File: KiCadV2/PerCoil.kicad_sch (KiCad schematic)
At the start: 22 parts, among them U14 74LV08AT14-13, U18 MX3502S, U22 DMHT10H032LFJ, U23 INA240A1D

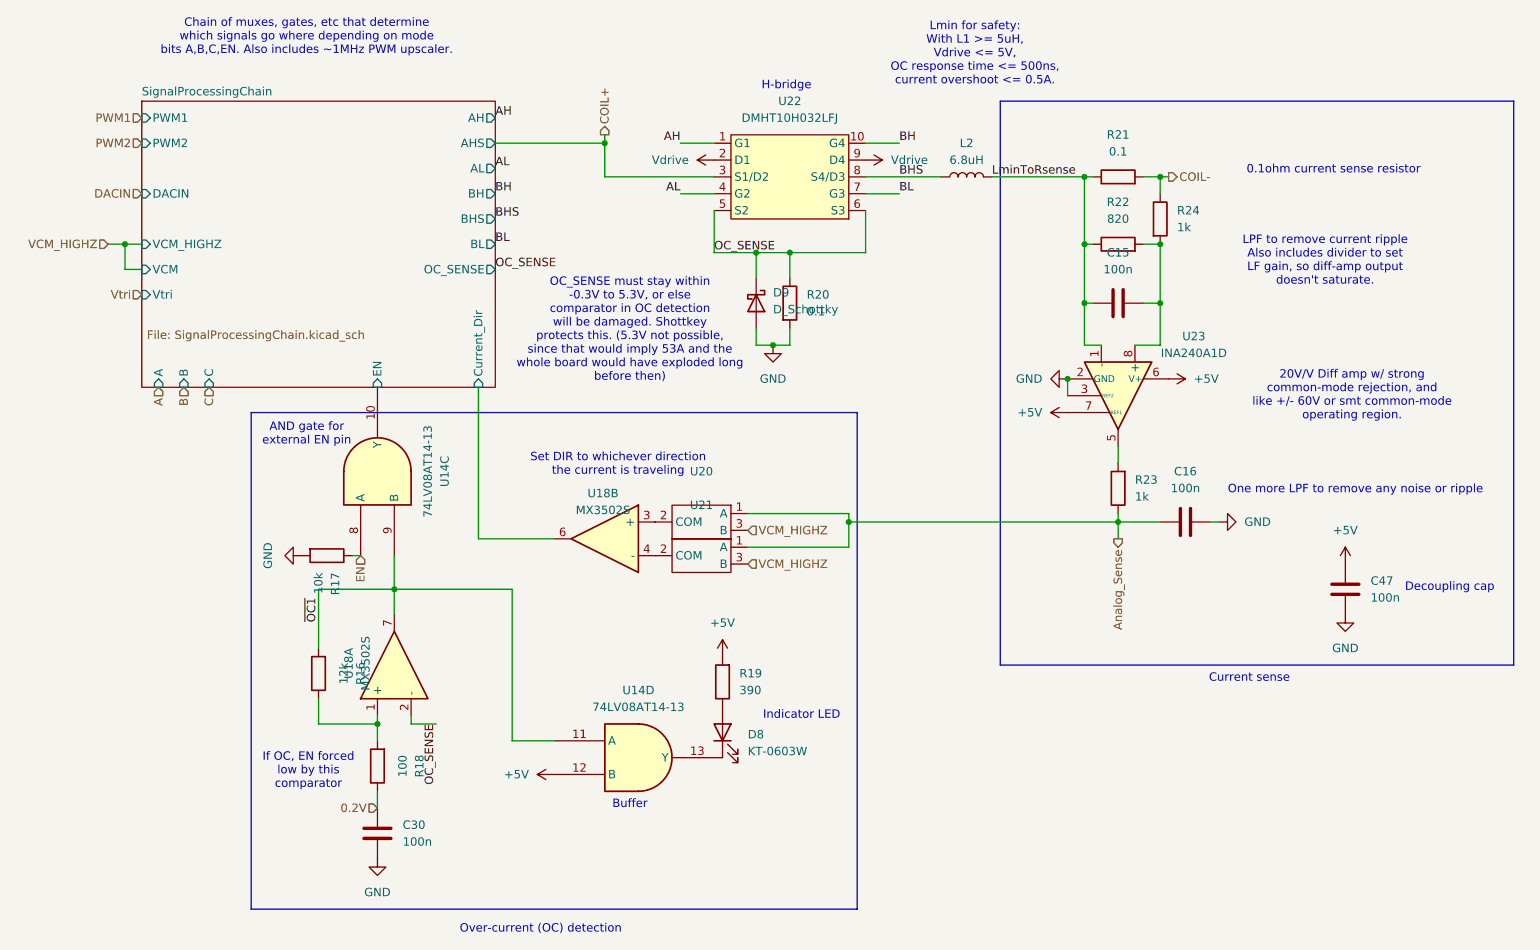
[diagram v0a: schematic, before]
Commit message: Made changes to schematic and just updated PCB from schematic. Haven't edited PCB yet.
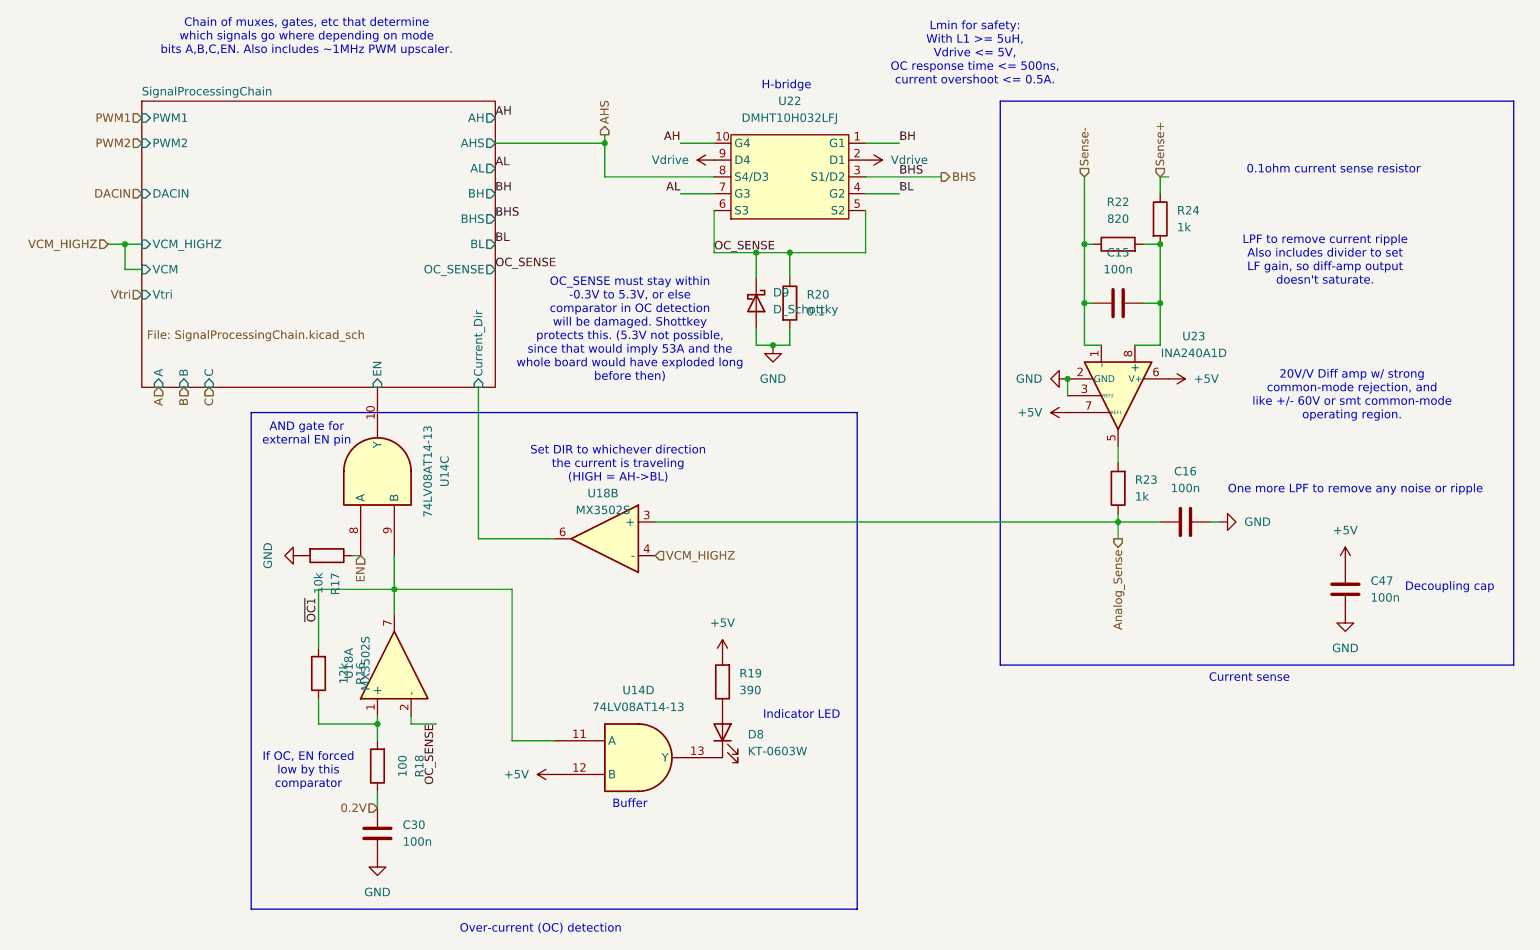
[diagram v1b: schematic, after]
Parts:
- removed L2: 6.8uH, Inductor_SMD:6.8uH C5127257, symbol Device:L
- removed R21: 0.1, Resistor_SMD:R_1206_3216Metric, symbol Device:R
- removed U20, U21: ~, TestPoint:SPDT_solder_bridge, symbol Connector:SPDT_solder_bridge
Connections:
- net COIL+ is gone; now on net BHS: U22.3 (S1/D2)
- net AH: now also U22.10 (G4); no longer U22.1 (G1)
- net AL: now also U22.7 (G3); no longer U22.4 (G2)
- net Analog_Sense: now also U18.3 (+)
- net BH: now also U22.1 (G1); no longer U22.10 (G4)
- net BHS: no longer U22.8 (S4/D3)
- net BL: now also U22.4 (G2); no longer U22.7 (G3)
- net VCM_HIGHZ: now also U18.4 (-)
- net COIL- renamed Sense+
- net LminToRsense renamed Sense-
- new net AHS: U22.8 (S4/D3)
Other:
- note added: "Set DIR to whichever direction the current is traveling (HIGH = AH->BL)"
- note removed: "Set DIR to whichever direction the current is traveling"
- moved on the sheet: U22

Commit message: Fixed AND Gate pins, added extra DAC logic Mux
DAC logic mux not yet done on PCB
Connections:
- net +5V: now also U14.13 (A); no longer U14.12 (B)
- net EN: now also U14.9 (B); no longer U14.8 (A)
- net SignalProcessingChain/EN: now also U14.8 (Y); no longer U14.10 (Y)
- net ~{OC1}: now also U14.10 (A), U14.12 (B); no longer U14.11 (A), U14.9 (B)
- net at D8.1 (K): now also U14.11 (Y); no longer U14.13 (Y)
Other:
- moved on the sheet: R17
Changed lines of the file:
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@@
+	)
+	(junction
+		(at 73.66 123.19)
+		(diameter 0)
+		(color 0 0 0 0)
 	)
 	(junction
@@
 	(wire
 		(pts
-			(xy 96.52 123.19) (xy 96.52 146.05)
-		)
-		(stroke
-			(width 0)
-			(type default)
-		)
-	)
-	(wire
-		(pts
 			(xy 182.88 71.12) (xy 182.88 80.01)
 		)
@@
 	(wire
 		(pts
-			(xy 78.74 118.11) (xy 78.74 123.19)
-		)
-		(stroke
-			(width 0)
-			(type default)
-		)
-	)
-	(wire
-		(pts
 			(xy 149.86 63.5) (xy 154.94 63.5)
 		)
@@
 	(wire
 		(pts
+			(xy 73.66 123.19) (xy 67.31 123.19)
+		)
+		(stroke
+			(width 0)
+			(type default)
+		)
+	)
+	(wire
+		(pts
 			(xy 135.89 86.36) (xy 138.43 86.36)
 		)
@@
 	(wire
 		(pts
-			(xy 73.66 118.11) (xy 72.39 118.11)
-		)
-		(stroke
-			(width 0)
-			(type default)
-		)
-	)
-	(wire
-		(pts
 			(xy 191.77 80.01) (xy 194.31 80.01)
 		)
@@
 	(wire
 		(pts
+			(xy 96.52 123.19) (xy 96.52 151.13)
+		)
+		(stroke
+			(width 0)
+			(type default)
+		)
+	)
+	(wire
+		(pts
 			(xy 127 66.04) (xy 127 72.39)
 		)
@@
 	(wire
 		(pts
+			(xy 78.74 119.38) (xy 82.55 119.38)
+		)
+		(stroke
+			(width 0)
+			(type default)
+		)
+	)
+	(wire
+		(pts
 			(xy 194.31 71.12) (xy 191.77 71.12)
 		)
@@
 	(wire
 		(pts
+			(xy 73.66 118.11) (xy 73.66 123.19)
+		)
+		(stroke
+			(width 0)
+			(type default)
+		)
+	)
+	(wire
+		(pts
 			(xy 110.49 60.96) (xy 127 60.96)
 		)
@@
 	(wire
 		(pts
-			(xy 78.74 123.19) (xy 67.31 123.19)
+			(xy 78.74 123.19) (xy 73.66 123.19)
 		)
 		(stroke
@@
 	(wire
 		(pts
-			(xy 96.52 146.05) (xy 102.87 146.05)
-		)
-		(stroke
-			(width 0)
-			(type default)
-		)
-	)
-	(wire
-		(pts
 			(xy 149.86 55.88) (xy 154.94 55.88)
 		)
@@
 	(wire
 		(pts
+			(xy 78.74 119.38) (xy 78.74 118.11)
+		)
+		(stroke
+			(width 0)
+			(type default)
+		)
+	)
+	(wire
+		(pts
 			(xy 91.44 115.57) (xy 102.87 115.57)
 		)
@@
 		(pts
 			(xy 190.5 86.36) (xy 194.31 86.36)
+		)
+		(stroke
+			(width 0)
+			(type default)
+		)
+	)
+	(wire
+		(pts
+			(xy 96.52 151.13) (xy 102.87 151.13)
 		)
 		(stroke
@@
 	(hierarchical_label "EN"
 		(shape input)
-		(at 73.66 118.11 270)
-		(effects
-			(font
-				(size 1.27 1.27)
-			)
-			(justify right)
+		(at 81.28 119.38 90)
+		(effects
+			(font
+				(size 1.27 1.27)
+			)
+			(justify left)
 		)
 	)
@@
 	(symbol
 		(lib_id "Device:R")
-		(at 68.58 118.11 270)
+		(at 86.36 119.38 90)
 		(unit 1)
 		(exclude_from_sim no)
@@
 		(dnp no)
 		(property "Reference" "R17"
-			(at 69.8501 120.65 0)
+			(at 85.0899 116.84 0)
 			(effects
 				(font
@@
 		)
 		(property "Value" "10k"
-			(at 67.3101 120.65 0)
+			(at 87.6299 116.84 0)
 			(effects
 				(font
@@
 		)
 		(property "Footprint" "Resistor_SMD:R_0603_1608Metric"
-			(at 68.58 116.332 90)
+			(at 86.36 121.158 90)
 			(effects
 				(font
@@
 		)
 		(property "Datasheet" "~"
-			(at 68.58 118.11 0)
+			(at 86.36 119.38 0)
 			(effects
 				(font
@@
 		)
 		(property "Description" "Resistor"
-			(at 68.58 118.11 0)
+			(at 86.36 119.38 0)
 			(effects
 				(font
@@
 		)
 		(property "LCSC" "C25804"
-			(at 68.58 118.11 0)
+			(at 86.36 119.38 0)
 			(effects
 				(font
@@
 	(symbol
 		(lib_id "power:+5V")
-		(at 102.87 151.13 90)
+		(at 102.87 146.05 90)
 		(unit 1)
 		(exclude_from_sim no)
@@
 		(fields_autoplaced yes)
 		(property "Reference" "#PWR052"
-			(at 106.68 151.13 0)
+			(at 106.68 146.05 0)
 			(effects
 				(font
@@
 		)
 		(property "Value" "+5V"
-			(at 99.06 151.1299 90)
+			(at 99.06 146.0499 90)
 			(effects
 				(font
@@
 		)
 		(property "Footprint" ""
-			(at 102.87 151.13 0)
+			(at 102.87 146.05 0)
 			(effects
 				(font
@@
 		)
 		(property "Datasheet" ""
-			(at 102.87 151.13 0)
+			(at 102.87 146.05 0)
 			(effects
 				(font
@@
 		)
 		(property "Description" "Power symbol creates a global label with name \"+5V\""
-			(at 102.87 151.13 0)
+			(at 102.87 146.05 0)
 			(effects
 				(font
@@
 	(symbol
 		(lib_id "power:GND")
-		(at 64.77 118.11 270)
+		(at 90.17 119.38 90)
 		(unit 1)
 		(exclude_from_sim no)
@@
 		(fields_autoplaced yes)
 		(property "Reference" "#PWR051"
-			(at 58.42 118.11 0)
+			(at 96.52 119.38 0)
 			(effects
 				(font
@@
 		)
 		(property "Value" "GND"
-			(at 59.69 118.11 0)
+			(at 95.25 119.38 0)
 			(effects
 				(font
@@
 		)
 		(property "Footprint" ""
-			(at 64.77 118.11 0)
+			(at 90.17 119.38 0)
 			(effects
 				(font
@@
 		)
 		(property "Datasheet" ""
-			(at 64.77 118.11 0)
+			(at 90.17 119.38 0)
 			(effects
 				(font
@@
 		)
 		(property "Description" "Power symbol creates a global label with name \"GND\" , ground"
-			(at 64.77 118.11 0)
-			(effects
-				(font
+			(at 90.17 119.38 0)
+			(effects
+				(font
